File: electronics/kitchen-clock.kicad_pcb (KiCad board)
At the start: 2 copper layers, 58.6 x 90.9 mm, 59 parts, among them IC1 CN3058E, IC2 HY2112, J1 USB_B_Micro, J2 INDICATORS, J3 PWR, J4 USB, J5 PWR, Q1 FS8205, Q2 2N7002, Q3 2N7002, SW1 SW_SPDT, U1 MT3608, U2 INA219AxD

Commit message: First draft of schematic and PCB of controller board
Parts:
- removed the D1 at (75.0, 107.0)
- removed the D2 at (75.1, 113.3)
- removed H1, H2, H3, H4: MountingHole, Chof747 Footprints:MountingHole_3.2mm_M3-smallBorder
- removed JP1: A1_H, Jumper:SolderJumper-2_P1.3mm_Open_RoundedPad1.0x1.5mm
- removed JP2: A1_L, Jumper:SolderJumper-2_P1.3mm_Open_RoundedPad1.0x1.5mm
- removed JP3: A0_H, Jumper:SolderJumper-2_P1.3mm_Open_RoundedPad1.0x1.5mm
- removed JP4: A0_L, Jumper:SolderJumper-2_P1.3mm_Open_RoundedPad1.0x1.5mm
- removed TP1: GND, TestPoint:TestPoint_Pad_2.0x2.0mm
- removed TP10: CHG, TestPoint:TestPoint_Pad_2.0x2.0mm
- removed TP2: VBAT, TestPoint:TestPoint_Pad_2.0x2.0mm
- removed TP3: BAT+, TestPoint:TestPoint_Pad_2.0x2.0mm
- removed TP4: BAT-, TestPoint:TestPoint_Pad_2.0x2.0mm
- removed TP5: 5V, TestPoint:TestPoint_Pad_2.0x2.0mm
- removed TP6: FDBK, TestPoint:TestPoint_Pad_2.0x2.0mm
- removed TP7: VBUS, TestPoint:TestPoint_Pad_2.0x2.0mm
- removed TP8: VREF, TestPoint:TestPoint_Pad_2.0x2.0mm
- removed TP9: RDY, TestPoint:TestPoint_Pad_2.0x2.0mm
- added BZ1: Buzzer, Chof747 Footprints:PS1240P02BT, F.Cu at (174.3, 112.8)
- added C10: 20p, Capacitor_SMD:C_0603_1608Metric_Pad1.08x0.95mm_HandSolder, F.Cu at (152.4, 97.2)
- added C11: 20p, Capacitor_SMD:C_0603_1608Metric_Pad1.08x0.95mm_HandSolder, F.Cu at (154.9, 97.2)
- added C6: 1uF, Capacitor_SMD:C_0603_1608Metric_Pad1.08x0.95mm_HandSolder, F.Cu at (136.8, 42.6)
- added C7: 10uF, Capacitor_SMD:C_0603_1608Metric_Pad1.08x0.95mm_HandSolder, F.Cu at (153.5, 71.4)
- added C8: 1uF, Capacitor_SMD:C_0603_1608Metric_Pad1.08x0.95mm_HandSolder, F.Cu at (170.1, 137.2)
- added C9: 1uF, Capacitor_SMD:C_0603_1608Metric_Pad1.08x0.95mm_HandSolder, F.Cu at (170.1, 144.3)
- added IC3: ESP32-S3-WROOM-1-N8R8, Chof747 Footprints:ESP32S3WROOM1N8R8, F.Cu at (165.4, 75.8)
- added IC4: ME6211C33M5G-N, Chof747 Footprints:SOT95P270X145-5N, F.Cu at (170.0, 140.7)
- added J6: CONN_DISPL, Connector_PinSocket_2.54mm:PinSocket_1x08_P2.54mm_Vertical, F.Cu at (183.8, 74.3)
- added J7: CONN_SERVO, Connector_PinSocket_2.54mm:PinSocket_1x03_P2.54mm_Vertical, F.Cu at (183.7, 99.4)
- added J8: CONN_PGR, Connector_PinSocket_2.54mm:PinSocket_1x04_P2.54mm_Vertical, F.Cu at (189.1, 53.1)
- added Q4: SS8050-G, Package_TO_SOT_SMD:SOT-23, F.Cu at (167.4, 95.3)
- added Q5: SS8050-G, Package_TO_SOT_SMD:SOT-23, F.Cu at (167.4, 100.1)
- added Q6: SS8050-G, Package_TO_SOT_SMD:SOT-23, F.Cu at (167.4, 105.8)
- added Q7: AO3401A, Package_TO_SOT_SMD:SOT-23, F.Cu at (171.6, 95.3)
- added Q8: AO3401A, Package_TO_SOT_SMD:SOT-23, F.Cu at (171.6, 100.1)
- added R15: 1k, Resistor_SMD:R_0603_1608Metric_Pad0.98x0.95mm_HandSolder, F.Cu at (157.6, 93.7)
- added R16: 1k, Resistor_SMD:R_0603_1608Metric_Pad0.98x0.95mm_HandSolder, F.Cu at (159.4, 93.7)
- added R17: 10k, Resistor_SMD:R_0603_1608Metric_Pad0.98x0.95mm_HandSolder, F.Cu at (180.0, 120.2)
- added R18: 1k, Resistor_SMD:R_0603_1608Metric_Pad0.98x0.95mm_HandSolder, F.Cu at (163.1, 93.7)
- added R19: 10k, Resistor_SMD:R_0603_1608Metric_Pad0.98x0.95mm_HandSolder, F.Cu at (176.8, 95.7)
- added R20: 1k, Resistor_SMD:R_0603_1608Metric_Pad0.98x0.95mm_HandSolder, F.Cu at (161.3, 93.7)
- added R21: 1k, Resistor_SMD:R_0603_1608Metric_Pad0.98x0.95mm_HandSolder, F.Cu at (171.3, 104.8)
- added R22: 10k, Resistor_SMD:R_0603_1608Metric_Pad0.98x0.95mm_HandSolder, F.Cu at (176.7, 97.6)
- added R23: 2k, Resistor_SMD:R_0603_1608Metric_Pad0.98x0.95mm_HandSolder, F.Cu at (181.6, 50.7)
- added R24: 2k, Resistor_SMD:R_0603_1608Metric_Pad0.98x0.95mm_HandSolder, F.Cu at (169.6, 50.6)
- added R25: 10k, Resistor_SMD:R_0603_1608Metric_Pad0.98x0.95mm_HandSolder, F.Cu at (152.9, 82.0)
- added R26: 10k, Resistor_SMD:R_0603_1608Metric_Pad0.98x0.95mm_HandSolder, F.Cu at (152.9, 83.6)
- added R27: 22, Resistor_SMD:R_0603_1608Metric_Pad0.98x0.95mm_HandSolder, F.Cu at (152.4, 93.7)
- added R28: 22, Resistor_SMD:R_0603_1608Metric_Pad0.98x0.95mm_HandSolder, F.Cu at (154.9, 93.7)
- added SW2: Reset, Chof747 Footprints:1TS003B-2500-3500A-CT (SMD Right Angle Tactile Switch), F.Cu at (136.7, 39.5)
- added U3: USBLC6-2SC6, Package_TO_SOT_SMD:SOT-23-6, F.Cu at (183.2, 124.8)
- added U4: ADS1115IDGS, Package_SO:TSSOP-10_3x3mm_P0.5mm, F.Cu at (174.7, 53.1)
- D2: renamed from D4; footprint LED_SMD:LED_0603_1608Metric_Pad1.05x0.95mm_HandSolder -> Capacitor_SMD:C_0603_1608Metric_Pad1.08x0.95mm_HandSolder
- J2: value INDICATORS -> Temp 1; footprint Connector_PinHeader_2.54mm:PinHeader_1x06_P2.54mm_Horizontal -> Chof747 Footprints:MJ2509N
- J3: value PWR -> Temp 2; footprint Connector_PinHeader_2.54mm:PinHeader_1x02_P2.54mm_Horizontal -> Chof747 Footprints:MJ2509N
- J4: value USB -> CONN_MOD; footprint Connector_PinHeader_2.54mm:PinHeader_1x02_P2.54mm_Horizontal -> Connector_PinSocket_2.54mm:PinSocket_1x02_P2.54mm_Vertical
- J5: value PWR -> CONN_ENC; footprint Chof747_Connectors:pad_1x2_1.5mmx3mm -> Connector_PinSocket_2.54mm:PinSocket_1x05_P2.54mm_Vertical
- R1: value 1k -> 10k
- moved J5 133.5 mm to (183.8, 57.5)
- moved R14 123.0 mm to (187.1, 129.3)
- moved D3 118.8 mm to (187.1, 131.1), turned to 0 degrees
- moved J1 115.3 mm to (190.1, 123.8), turned to 90 degrees
- moved R3 109.8 mm to (185.6, 143.2), turned to -90 degrees
- moved NT1 109.6 mm to (186.8, 120.9), turned to 90 degrees
- moved J2 107.8 mm to (182.2, 44.0), turned to 180 degrees
- moved C1 103.7 mm to (182.9, 138.0), turned to 180 degrees
- moved R4 103.3 mm to (178.7, 130.5)
- moved R9 103.3 mm to (184.1, 130.5)
- moved Q2 103.3 mm to (181.2, 130.5)
- moved R12 101.8 mm to (163.4, 136.1), turned to -90 degrees
- moved IC1 100.0 mm to (180.8, 141.7), turned to 180 degrees
- moved R11 99.7 mm to (161.9, 136.1), turned to 90 degrees
- moved C3 97.3 mm to (159.1, 132.1), turned to 180 degrees
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- renumbered D3 to D1, D5 to D3
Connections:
- net /boosted renamed /Battery Management/boosted
- net BAT+ renamed /Battery Management/BAT+
- net BAT- renamed /Battery Management/BAT-
- net CHG_IND renamed /Battery Management/CHG_IND
- net RDY_IND renamed /Battery Management/RDY_IND
- net VBAT renamed /Battery Management/VBAT
- net VBAT_M renamed /Battery Management/VBAT_M
- J2 pad 1: VREF -> GND
- J2 pad 2: Net-(J2-Pin_2) -> /Peripherals/TEMP0
- J2 pad 3: Net-(J2-Pin_3) -> /Peripherals/TEMP0
- J3 pad 1: +5V -> GND
- J3 pad 2: GND -> /Peripherals/TEMP1
- J4 pad 1: USB_N -> GND
- J4 pad 2: USB_P -> /Peripherals/MODE_BUTTON
- J5 pad 1: VBUS -> GND
- J5 pad 2: GND -> +3V3
- Q2 pad 3: Net-(J2-Pin_3) -> /Battery Management/READY
- Q3 pad 3: Net-(J2-Pin_2) -> /Battery Management/CHARGE
- R1 pad 1: VBUS -> +3V3
- R8 pad 1: VREF -> +3V3
- R8 pad 2: Net-(J2-Pin_2) -> /Battery Management/CHARGE
- R9 pad 1: VREF -> +3V3
- R9 pad 2: Net-(J2-Pin_3) -> /Battery Management/READY
- U2 pad 1: Net-(JP1-A) -> GND
- U2 pad 2: Net-(JP3-A) -> GND
- U2 pad 5: VREF -> +3V3
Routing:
- net +3V3: track 0.00 -> 224.2 mm, vias 0 -> 4
- net VREF: track 86.5 -> 0.00 mm, vias 1 -> 0
- net SDA: track 21.8 -> 92.0 mm, vias 0 -> 2
- net /Battery Management/READY: track 0.00 -> 69.1 mm, vias 0 -> 6
- net /Battery Management/CHARGE: track 0.00 -> 64.1 mm, vias 0 -> 6
- net SCL: track 24.9 -> 88.7 mm, vias 0 -> 2
- net /Battery Management/BAT-: track 98.4 -> 38.8 mm
- net /Microcontroller & Controls/ADC0_DRV_IO8: track 0.00 -> 51.3 mm, vias 0 -> 4
- net /Microcontroller & Controls/USBPROT_N: track 0.00 -> 50.5 mm, vias 0 -> 2
- net /Microcontroller & Controls/USBPROT_P: track 0.00 -> 49.7 mm, vias 0 -> 2
- net /Microcontroller & Controls/ADC1_DRV_IO9: track 0.00 -> 49.4 mm, vias 0 -> 4
- net /Peripherals/MODE_BUTTON: track 0.00 -> 47.1 mm
- net Net-(IC3-IO0): track 0.00 -> 46.3 mm, vias 0 -> 2
- net Net-(IC3-EN): track 6.15 -> 49.4 mm, vias 0 -> 4
- net GND: track 69.5 -> 27.7 mm, vias 16 -> 18
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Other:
- board size 58.6 x 90.9 mm -> 66.9 x 110 mm
- board text added: "KitchenClock v1.0 (2024)"
- board text removed: "Battery Power (LiFePo4) v1.0 (2024)"
- board text removed: "CHG IND"
- board text removed: "Charging"
- board text removed: "D+"
- board text removed: "D-"
- board text removed: "INA219 Adr."
- board text removed: "RDY IND"
- board text removed: "Ready"
- board text removed: "SCL(I2C)"
- board text removed: "SDA(I2C)"
- board text removed: "USB"
- board text removed: "VBUS"
- board text removed: "VREF"

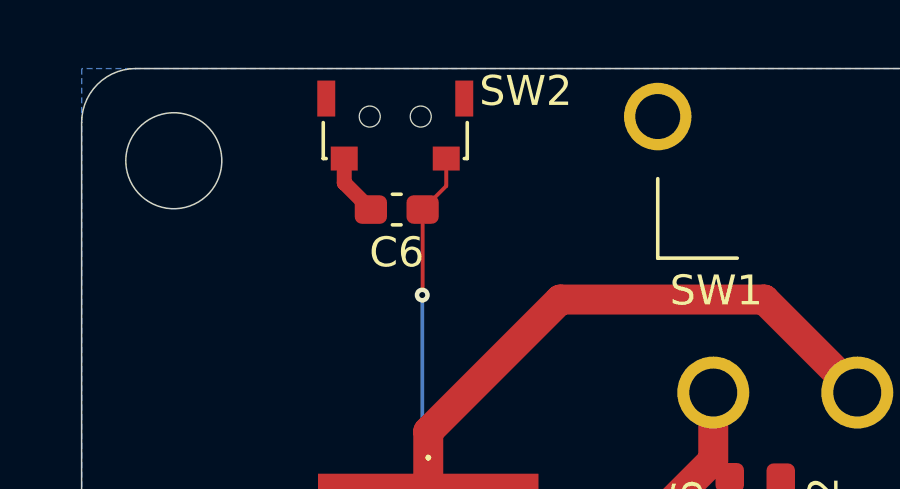
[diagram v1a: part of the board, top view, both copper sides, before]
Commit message: changed footprint of reset button
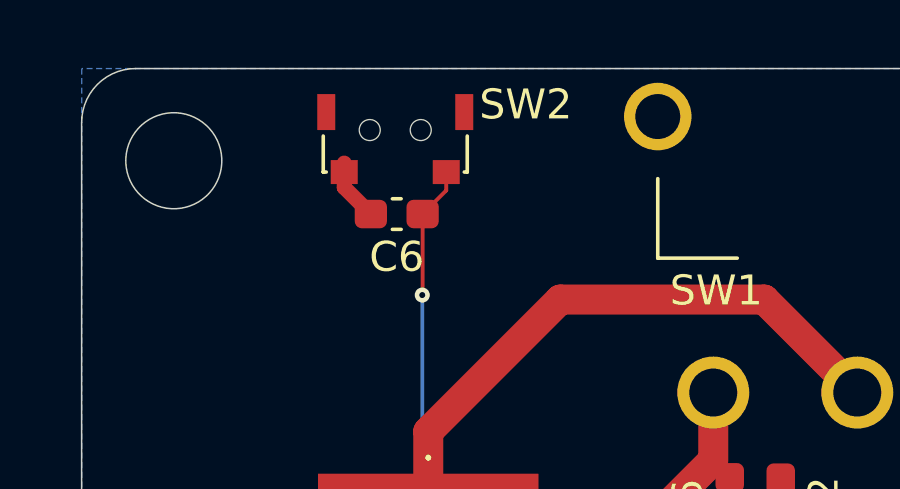
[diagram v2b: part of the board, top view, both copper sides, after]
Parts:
- moved SW2 0.45 mm to (136.7, 39.9)
- moved C6 0.15 mm to (136.8, 42.7)
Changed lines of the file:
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@@
 	(footprint "Chof747 Footprints:1TS003B-2500-3500A-CT (SMD Right Angle Tactile Switch)"
 		(layer "F.Cu")
-		(at 136.7 39.474656)
+		(at 136.7 39.924656)
 		(property "Reference" "SW2"
 			(at 4.35 -0.85 0)
@@
 		)
 		(fp_rect
-			(start -2.6 -1.6)
+			(start -2.6 -1.4)
 			(end 2.6 1.9)
 			(stroke
@@
 			(thermal_bridge_angle 45)
 		)
+		(model "${USERMODELS}/3dmodels/2x4 tactile smd switch.step"
+			(offset
+				(xyz 0 0 0)
+			)
+			(scale
+				(xyz 1 1 1)
+			)
+			(rotate
+				(xyz 0 0 0)
+			)
+		)
 	)
 	(footprint "Chof747 Footprints:MJ2509N"
@@
 	(footprint "Capacitor_SMD:C_0603_1608Metric_Pad1.08x0.95mm_HandSolder"
 		(layer "F.Cu")
-		(at 136.75 42.574656 180)
+		(at 136.75 42.724656 180)
 		(descr "Capacitor SMD 0603 (1608 Metric), square (rectangular) end terminal, IPC_7351 nominal with elongated pad for handsoldering. (Body size source: IPC-SM-782 page 76, https://www.pcb-3d.com/wordpress/wp-content/uploads/ipc-sm-782a_amendment_1_and_2.pdf), generated with kicad-footprint-generator")
 		(tags "capacitor handsolder")
@@
 	)
 	(segment
-		(start 135 40.874656)
-		(end 135 41.687156)
+		(start 135 41.024656)
+		(end 135 41.837156)
 		(width 0.5)
 		(layer "F.Cu")
@@
 	)
 	(segment
-		(start 135 41.687156)
-		(end 135.8875 42.574656)
+		(start 135 41.837156)
+		(end 135.8875 42.724656)
 		(width 0.5)
 		(layer "F.Cu")
@@
 	)
 	(segment
-		(start 137.6125 42.574656)
-		(end 138.4 41.787156)
+		(start 137.6125 42.724656)
+		(end 138.4 41.937156)
 		(width 0.13)
 		(layer "F.Cu")
@@
 	)
 	(segment
-		(start 138.4 41.787156)
-		(end 138.4 40.874656)
+		(start 138.4 41.937156)
+		(end 138.4 41.024656)
 		(width 0.13)
 		(layer "F.Cu")

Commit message: performed CRC check and fixed errors
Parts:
- D2: footprint Capacitor_SMD:C_0603_1608Metric_Pad1.08x0.95mm_HandSolder -> LED_SMD:LED_0603_1608Metric_Pad1.05x0.95mm_HandSolder
- moved D2 0.15 mm to (149.7, 52.4)
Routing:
- net /Battery Management/BAT+: track 160.8 -> 188.2 mm
- net GND: track 27.7 -> 41.9 mm, vias 18 -> 30
- net Net-(D2-A): track 0.00 -> 1.86 mm
- net Net-(D3-A): track 0.00 -> 1.77 mm
- net /Battery Management/BAT-: track 38.8 -> 40.4 mm
- net Net-(J1-Shield): track 15.0 -> 16.2 mm
- net /Microcontroller & Controls/ADC0_DRV_IO8: track 51.3 -> 51.9 mm
- net +3V3: track 224.2 -> 223.6 mm

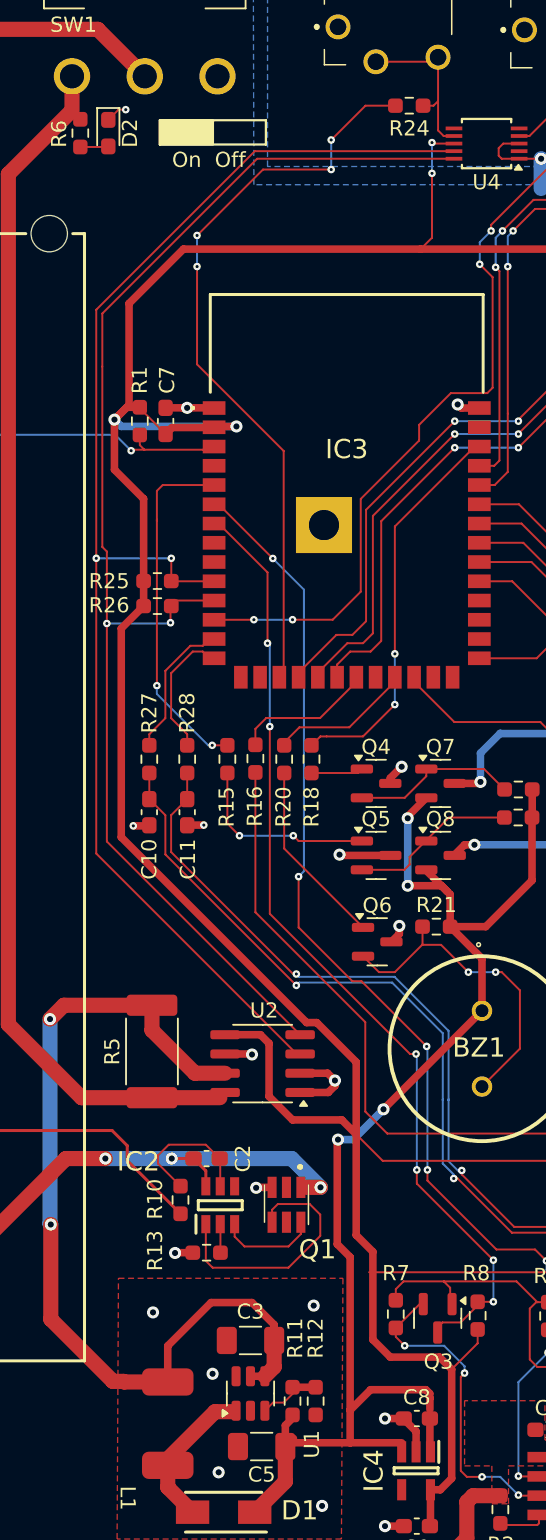
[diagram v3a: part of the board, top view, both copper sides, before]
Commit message: Performed CRC and DRC on board + corrections
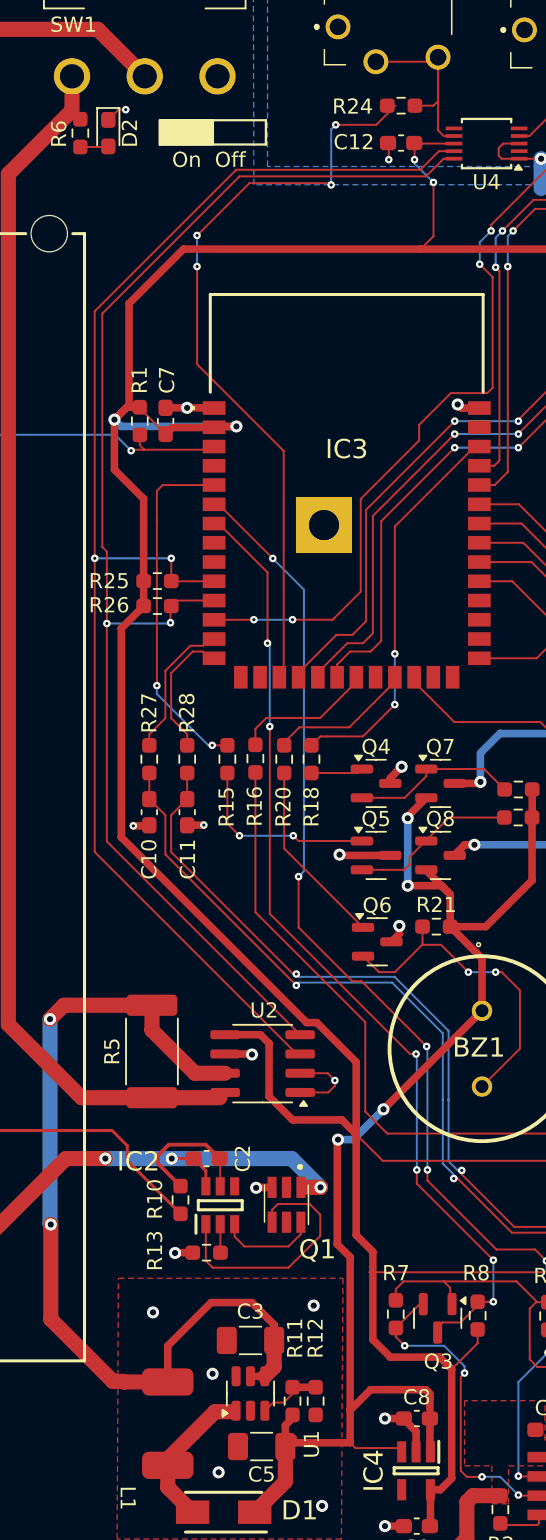
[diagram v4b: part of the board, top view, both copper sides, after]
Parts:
- added C12: 0.1uF, Capacitor_SMD:C_0603_1608Metric_Pad1.08x0.95mm_HandSolder, F.Cu at (169.0, 53.1)
- G***: footprint Chof747 Logos:LOGO small -> Chof747 Logos:LOGO large
- moved G*** 2.44 mm to (135.6, 97.5)
- moved R24 0.54 mm to (169.0, 50.6)
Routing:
- net +3V3: track 223.6 -> 225.3 mm
- net GND: track 41.9 -> 43.0 mm, vias 30 -> 31
- net /Microcontroller & Controls/ADC1_DRV_IO9: track 49.4 -> 50.5 mm
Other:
- board text added: "OK"
